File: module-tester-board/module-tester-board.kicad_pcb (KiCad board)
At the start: 2 copper layers, 69.1 x 53.3 mm, 29 parts, among them J2 Barrel_Jack, J4 Tester Points, U1 LT8330, U4 MCP2515, U5 ATA6560,1, Y1 20MHz

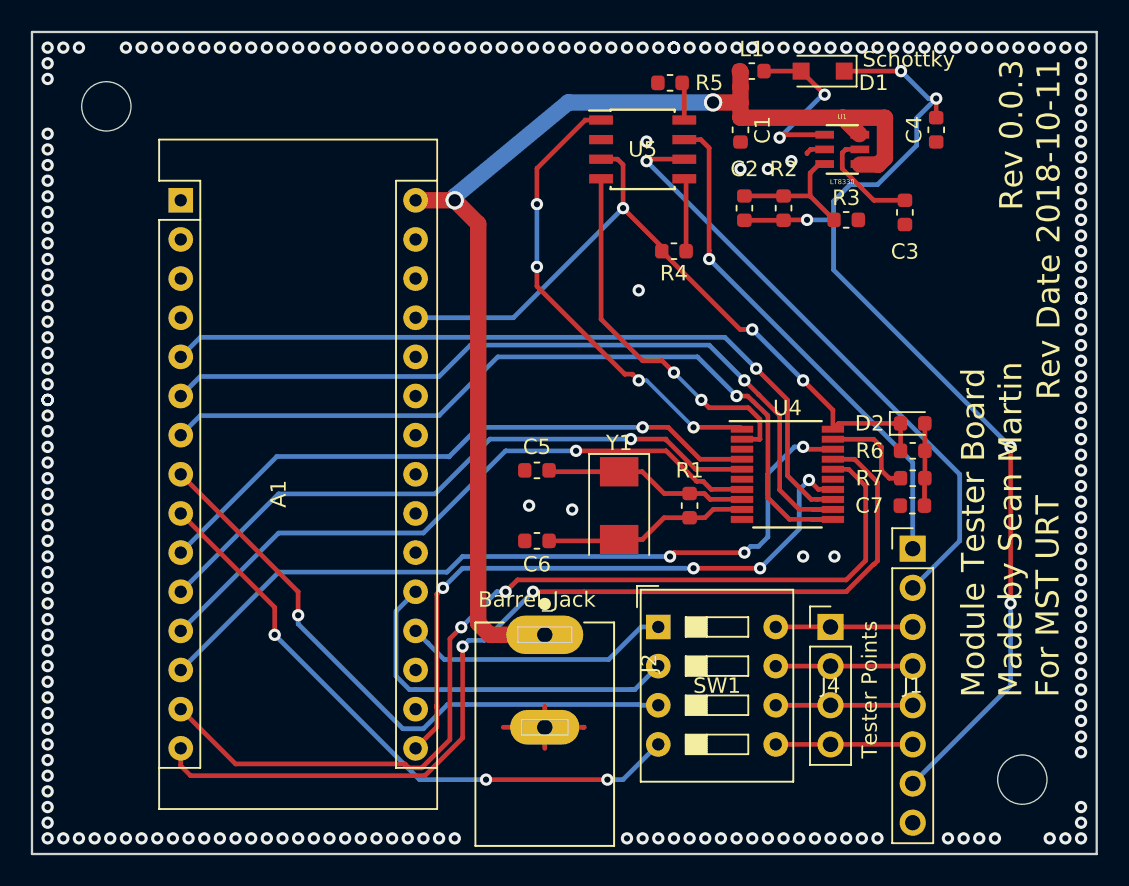
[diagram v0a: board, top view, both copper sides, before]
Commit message: Added 5v Regulator
Moved some parts to add additonal pin
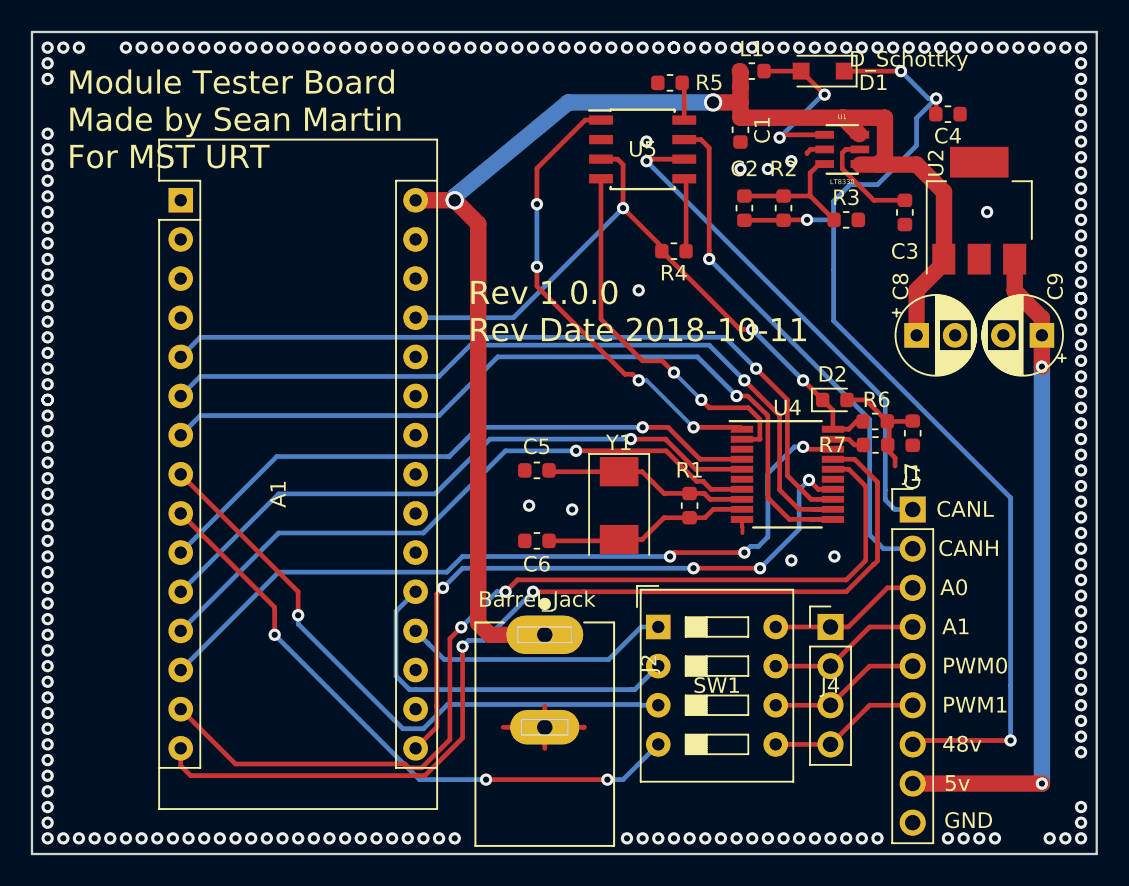
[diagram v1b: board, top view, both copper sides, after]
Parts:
- removed ? (x2): , MountingHole:MountingHole_3.2mm_M3
- removed the G*** at (152.9, 93.2)
- added C8: 100uF, Capacitor_THT:CP_Radial_D5.0mm_P2.50mm, F.Cu at (175.8, 86.2)
- added C9: 100uF, Capacitor_THT:CP_Radial_D5.0mm_P2.50mm, F.Cu at (183.9, 86.2)
- added G***: LOGO, logo:logo, B.Cu at (152.9, 93.2)
- added U2: L7805, Package_TO_SOT_SMD:SOT-223, F.Cu at (179.8, 78.1)
- D1: value Schottky -> D_Schottky
- J1: value (none) -> Conn_01x09; footprint Connector_PinHeader_2.54mm:PinHeader_1x08_P2.54mm_Vertical -> Connector_PinHeader_2.54mm:PinHeader_1x09_P2.54mm_Vertical
- J4: value Tester Points -> Conn_01x04_Male
- SW1: value (none) -> SW_DIP_x04
- U4: value MCP2515 -> MCP2515-EST
- moved D2 5.28 mm to (170.5, 90.4)
- moved C7 4.70 mm to (175.5, 92.6), turned to 270 degrees
- moved R7 3.24 mm to (173.1, 93.3)
- moved R6 3.09 mm to (173.1, 91.8)
- moved J1 2.54 mm to (175.5, 97.5)
- moved C4 1.27 mm to (177.8, 71.9), turned to 180 degrees
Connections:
- J1 pad 1: CANH -> CANL
- J1 pad 2: CANL -> CANH
- J1 pad 8: GND -> +5VD
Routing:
- net +5VD: track 0.00 -> 43.1 mm, vias 0 -> 2
- net +12V: track 75.0 -> 90.0 mm
- net CANL: track 39.9 -> 32.9 mm
- net Reset: track 6.33 -> 2.03 mm
- net +5V: track 48.1 -> 43.8 mm
- net Net-(C7-Pad1): track 5.34 -> 8.15 mm
- net Net-(J1-Pad6): track 8.89 -> 10.1 mm
- net Net-(J1-Pad5): track 8.89 -> 9.94 mm
- net +48V: track 77.1 -> 78.1 mm, vias 5 -> 4
- net CANH: track 33.3 -> 34.3 mm
- net Net-(J1-Pad3): track 8.89 -> 9.82 mm
- net Net-(J1-Pad4): track 8.89 -> 9.82 mm
- net GND: track 11.9 -> 12.7 mm, vias 225 -> 226
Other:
- board text added: "48v"
- board text added: "5v"
- board text added: "A0"
- board text added: "A1"
- board text added: "CANH"
- board text added: "CANL"
- board text added: "GND"
- board text added: "PWM0"
- board text added: "PWM1"
- board text added: "Rev 1.0.0 Rev Date 2018-10-11"
- board text removed: "Rev 0.0.3 Rev Date 2018-10-11"
